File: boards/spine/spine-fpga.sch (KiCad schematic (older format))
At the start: 24 parts, among them U7 iCE40-HX1K-TQ144

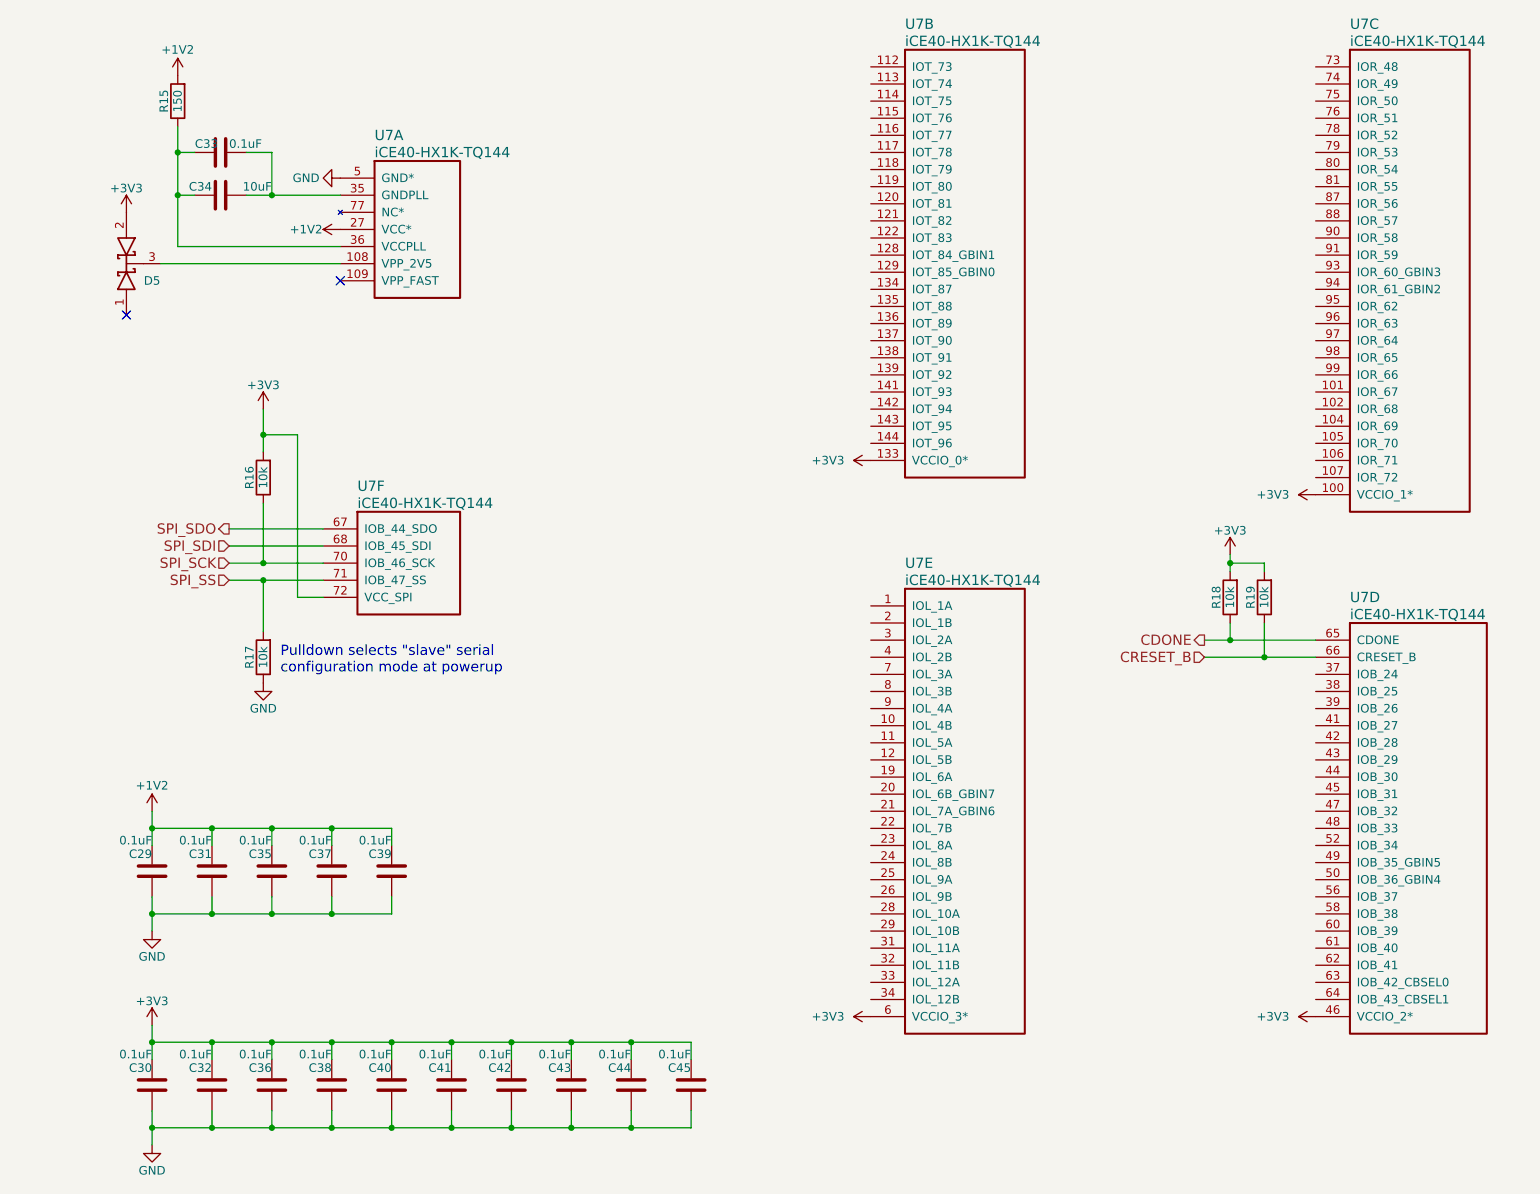
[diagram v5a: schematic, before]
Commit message: Early power management work
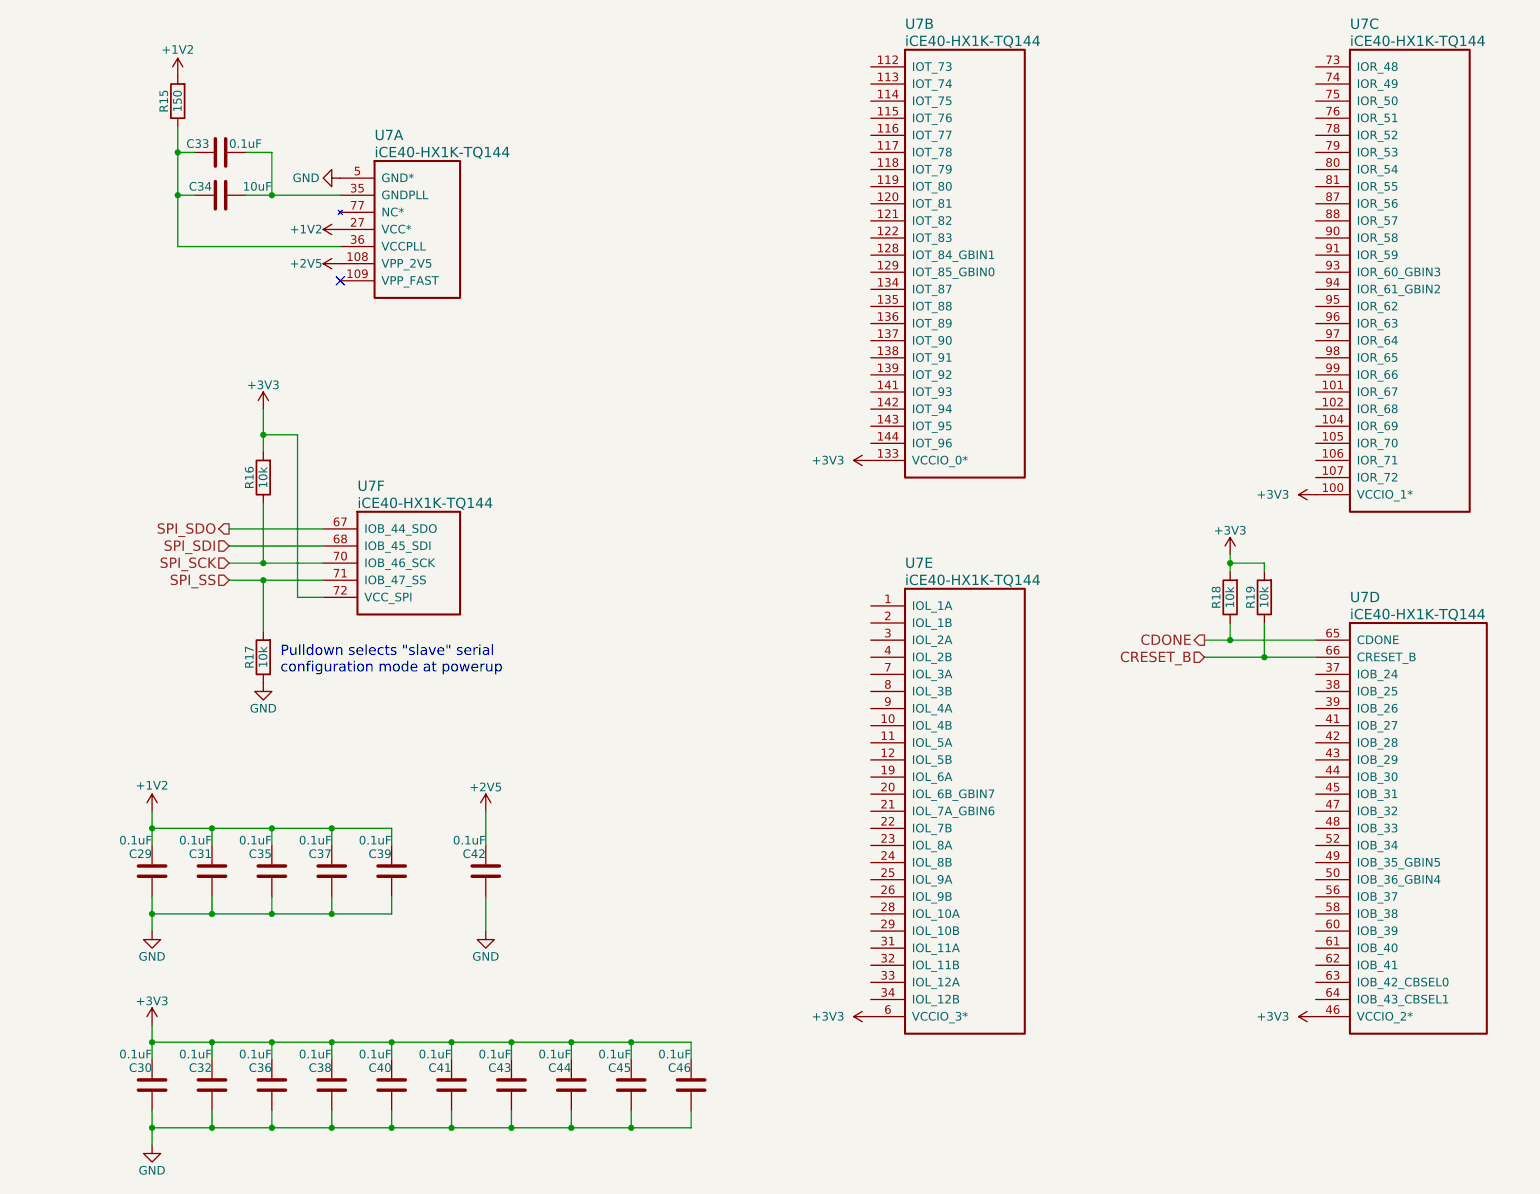
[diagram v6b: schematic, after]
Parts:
- removed D5: BAT54 2x common cathode, symbol D_Schottky_x2_KCom_AAK
- added C42: 0.1uF, 0805, symbol C
- renumbered C42 to C43, C43 to C44, C44 to C45, C45 to C46
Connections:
- net GND: now also C42.1
- net +2V5: now reaches U7.108 (VPP_2V5)
- net +2V5: now also C42.2
- no-connect marks 2 -> 1
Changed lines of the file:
@@
 $Descr USLetter 11000 8500
 encoding utf-8
-Sheet 5 5
+Sheet 5 6
 Title ""
 Date ""
@@
 $EndComp
 $Comp
-L GND #PWR0105
+L GND #PWR112
 U 1 1 56403C36
 P 3050 1550
-F 0 "#PWR0105" H 3050 1300 50  0001 C CNN
+F 0 "#PWR112" H 3050 1300 50  0001 C CNN
 F 1 "GND" V 3050 1350 50  0000 C CNN
 F 2 "" H 3050 1550 60  0000 C CNN
@@
 $EndComp
 $Comp
-L +1V2 #PWR0106
+L +1V2 #PWR113
 U 1 1 564083AC
 P 3050 1850
-F 0 "#PWR0106" H 3050 1700 50  0001 C CNN
+F 0 "#PWR113" H 3050 1700 50  0001 C CNN
 F 1 "+1V2" V 3050 2050 50  0000 C CNN
 F 2 "" H 3050 1850 60  0000 C CNN
@@
 	2100 1250 2100 1950
 $Comp
-L +1V2 #PWR0107
+L +1V2 #PWR109
 U 1 1 5640879A
 P 2100 950
-F 0 "#PWR0107" H 2100 800 50  0001 C CNN
+F 0 "#PWR109" H 2100 800 50  0001 C CNN
 F 1 "+1V2" H 2100 1100 50  0000 C CNN
 F 2 "" H 2100 950 60  0000 C CNN
@@
 	1    0    0    -1
 $EndComp
-$Comp
-L D_Schottky_x2_KCom_AAK D5
-U 1 1 5640B2EE
-P 1800 2050
-F 0 "D5" V 1700 1900 50  0000 C CNN
-F 1 "BAT54 2x common cathode" H 1800 2150 50  0001 C CNN
-F 2 "" H 1800 2050 60  0000 C CNN
-F 3 "http://www.diodes.com/_files/datasheets/ds11005.pdf" H 1800 2050 60  0001 C CNN
-F 4 "Diodes Inc" H 1800 2200 39  0001 C CNN "MfrId"
-F 5 "BAT54C-7-F" V 1800 2050 60  0001 C CNN "MfgId"
-F 6 "BAT54C-FDICT-ND" V 1800 2050 60  0001 C CNN "Vend1Id"
-F 7 ".03955" V 1800 2050 60  0001 C CNN "RefPrice1k"
-F 8 "Digikey" V 1800 2050 60  0001 C CNN "Vend1"
-	1    1800 2050
-	0    -1   -1   0
-$EndComp
 Wire Wire Line
 	2100 1950 3050 1950
-$Comp
-L +3V3 #PWR0108
-U 1 1 5640C82E
-P 1800 1750
-F 0 "#PWR0108" H 1800 1600 50  0001 C CNN
-F 1 "+3V3" H 1800 1890 50  0000 C CNN
-F 2 "" H 1800 1750 60  0000 C CNN
-F 3 "" H 1800 1750 60  0000 C CNN
-	1    1800 1750
-	1    0    0    -1
-$EndComp
 NoConn ~ 3050 2150
 $Comp
-L +3V3 #PWR0109
+L +3V3 #PWR118
 U 1 1 5640CF73
 P 6150 6450
-F 0 "#PWR0109" H 6150 6300 50  0001 C CNN
+F 0 "#PWR118" H 6150 6300 50  0001 C CNN
 F 1 "+3V3" V 6150 6700 50  0000 C CNN
 F 2 "" H 6150 6450 60  0000 C CNN
@@
 SPI_SS
 $Comp
-L +3V3 #PWR0110
+L +3V3 #PWR110
 U 1 1 5640D6CD
 P 2600 2900
-F 0 "#PWR0110" H 2600 2750 50  0001 C CNN
+F 0 "#PWR110" H 2600 2750 50  0001 C CNN
 F 1 "+3V3" H 2600 3040 50  0000 C CNN
 F 2 "" H 2600 2900 60  0000 C CNN
@@
 Connection ~ 2600 3050
 $Comp
-L GND #PWR0111
+L GND #PWR111
 U 1 1 5640DE11
 P 2600 4500
-F 0 "#PWR0111" H 2600 4250 50  0001 C CNN
+F 0 "#PWR111" H 2600 4250 50  0001 C CNN
 F 1 "GND" H 2600 4350 50  0000 C CNN
 F 2 "" H 2600 4500 60  0000 C CNN
@@
 $EndComp
 $Comp
-L +3V3 #PWR0112
+L +3V3 #PWR117
 U 1 1 5640E61C
 P 6150 3200
-F 0 "#PWR0112" H 6150 3050 50  0001 C CNN
+F 0 "#PWR117" H 6150 3050 50  0001 C CNN
 F 1 "+3V3" V 6150 3450 50  0000 C CNN
 F 2 "" H 6150 3200 60  0000 C CNN
@@
 $EndComp
 $Comp
-L +3V3 #PWR0113
+L +3V3 #PWR120
 U 1 1 5640E78F
 P 8750 3400
-F 0 "#PWR0113" H 8750 3250 50  0001 C CNN
+F 0 "#PWR120" H 8750 3250 50  0001 C CNN
 F 1 "+3V3" V 8750 3650 50  0000 C CNN
 F 2 "" H 8750 3400 60  0000 C CNN
@@
 $EndComp
 $Comp
-L +3V3 #PWR0114
+L +3V3 #PWR121
 U 1 1 5640E7E2
 P 8750 6450
-F 0 "#PWR0114" H 8750 6300 50  0001 C CNN
+F 0 "#PWR121" H 8750 6300 50  0001 C CNN
 F 1 "+3V3" V 8750 6700 50  0000 C CNN
 F 2 "" H 8750 6450 60  0000 C CNN
@@
 $EndComp
 $Comp
-L +1V2 #PWR0115
+L +1V2 #PWR105
 U 1 1 5640EE64
 P 1950 5250
-F 0 "#PWR0115" H 1950 5100 50  0001 C CNN
+F 0 "#PWR105" H 1950 5100 50  0001 C CNN
 F 1 "+1V2" H 1950 5400 50  0000 C CNN
 F 2 "" H 1950 5250 60  0000 C CNN
@@
 $EndComp
 $Comp
-L +3V3 #PWR0116
+L +3V3 #PWR107
 U 1 1 5640F3E2
 P 1950 6500
-F 0 "#PWR0116" H 1950 6350 50  0001 C CNN
+F 0 "#PWR107" H 1950 6350 50  0001 C CNN
 F 1 "+3V3" H 1950 6640 50  0000 C CNN
 F 2 "" H 1950 6500 60  0000 C CNN
@@
 Connection ~ 4750 7100
 $Comp
-L GND #PWR0117
+L GND #PWR106
 U 1 1 5640FDCB
 P 1950 5950
-F 0 "#PWR0117" H 1950 5700 50  0001 C CNN
+F 0 "#PWR106" H 1950 5700 50  0001 C CNN
 F 1 "GND" H 1950 5800 50  0000 C CNN
 F 2 "" H 1950 5950 60  0000 C CNN
@@
 $EndComp
 $Comp
-L GND #PWR0118
+L GND #PWR108
 U 1 1 5640FE24
 P 1950 7200
-F 0 "#PWR0118" H 1950 6950 50  0001 C CNN
+F 0 "#PWR108" H 1950 6950 50  0001 C CNN
 F 1 "GND" H 1950 7050 50  0000 C CNN
 F 2 "" H 1950 7200 60  0000 C CNN
@@
 Connection ~ 8450 4350
 $Comp
-L +3V3 #PWR0119
+L +3V3 #PWR119
 U 1 1 56410A99
 P 8250 3750
-F 0 "#PWR0119" H 8250 3600 50  0001 C CNN
+F 0 "#PWR119" H 8250 3600 50  0001 C CNN
 F 1 "+3V3" H 8250 3890 50  0000 C CNN
 F 2 "" H 8250 3750 60  0000 C CNN
@@
 $EndComp
 $Comp
-L C C42
+L C C43
 U 1 1 5642EDED
 P 4050 6850
-F 0 "C42" H 4050 6750 50  0000 L CNN
+F 0 "C43" H 4050 6750 50  0000 L CNN
 F 1 "0.1uF" H 4050 6700 50  0000 L TNN
 F 2 "0805" H 4088 6700 30  0001 C CNN
@@
 $EndComp
 $Comp
-L C C43
+L C C44
 U 1 1 5642EE46
 P 4400 6850
-F 0 "C43" H 4400 6750 50  0000 L CNN
+F 0 "C44" H 4400 6750 50  0000 L CNN
 F 1 "0.1uF" H 4400 6700 50  0000 L TNN
 F 2 "0805" H 4438 6700 30  0001 C CNN
@@
 $EndComp
 $Comp
-L C C44
+L C C45
 U 1 1 5642EEA2
 P 4750 6850
-F 0 "C44" H 4750 6750 50  0000 L CNN
+F 0 "C45" H 4750 6750 50  0000 L CNN
 F 1 "0.1uF" H 4750 6700 50  0000 L TNN
 F 2 "0805" H 4788 6700 30  0001 C CNN
@@
 $EndComp
 $Comp
-L C C45
+L C C46
 U 1 1 5642EF02
 P 5100 6850
-F 0 "C45" H 5100 6750 50  0000 L CNN
+F 0 "C46" H 5100 6750 50  0000 L CNN
 F 1 "0.1uF" H 5100 6700 50  0000 L TNN
 F 2 "0805" H 5138 6700 30  0001 C CNN
@@
 	-1   0    0    1
 $EndComp
-Wire Wire Line
-	2000 2050 3050 2050
-NoConn ~ 1800 2350
 $Comp
 L C C33
 U 1 1 5642F812
 P 2350 1400
-F 0 "C33" V 2300 1250 50  0000 L CNN
+F 0 "C33" V 2300 1200 50  0000 L CNN
 F 1 "0.1uF" V 2300 1450 50  0000 L CNN
 F 2 "0805" H 2388 1250 30  0001 C CNN
@@
 	2650 1400 2500 1400
 Connection ~ 2650 1650
+$Comp
+L +2V5 #PWR114
+U 1 1 5644292C
+P 3050 2050
+F 0 "#PWR114" H 3050 1900 50  0001 C CNN
+F 1 "+2V5" V 3050 2250 50  0000 C CNN
+F 2 "" H 3050 2050 60  0000 C CNN
+F 3 "" H 3050 2050 60  0000 C CNN
+	1    3050 2050
+	0    -1   -1   0
+$EndComp
+Wire Wire Line
+	3900 5250 3900 5450
+Wire Wire Line
+	3900 5750 3900 5950
+$Comp
+L GND #PWR116
+U 1 1 56443449
+P 3900 5950
+F 0 "#PWR116" H 3900 5700 50  0001 C CNN
+F 1 "GND" H 3900 5800 50  0000 C CNN
+F 2 "" H 3900 5950 60  0000 C CNN
+F 3 "" H 3900 5950 60  0000 C CNN
+	1    3900 5950
+	1    0    0    -1
+$EndComp
+$Comp
+L C C42
+U 1 1 56443455
+P 3900 5600
+F 0 "C42" H 3900 5500 50  0000 L CNN
+F 1 "0.1uF" H 3900 5450 50  0000 L TNN
+F 2 "0805" H 3938 5450 30  0001 C CNN
+F 3 "http://psearch.murata.com/capacitor/product/GRM21BR71H104MA01%23.pdf" H 3900 5600 60  0001 C CNN
+F 4 "0.01880" V 3900 5600 60  0001 C CNN "RefPrice1k"
+F 5 "490-9672-2-ND" V 3900 5600 60  0001 C CNN "Vend1Id"
+F 6 "Digikey" V 3900 5600 60  0001 C CNN "Vend1"
+F 7 "Murata" V 3900 5600 60  0001 C CNN "MfrId"
+F 8 "GRM21BR71H104MA01L" V 3900 5600 60  0001 C CNN "MfgId"
+	1    3900 5600
+	-1   0    0    1
+$EndComp
+$Comp
+L +2V5 #PWR115
+U 1 1 56443529
+P 3900 5250
+F 0 "#PWR115" H 3900 5100 50  0001 C CNN
+F 1 "+2V5" H 3900 5390 50  0000 C CNN
+F 2 "" H 3900 5250 60  0000 C CNN
+F 3 "" H 3900 5250 60  0000 C CNN
+	1    3900 5250
+	1    0    0    -1
+$EndComp
 $EndSCHEMATC
